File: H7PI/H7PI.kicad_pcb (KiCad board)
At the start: 4 copper layers, 65 x 30 mm, 52 parts, among them J1 XKTF-015-N, J10 DNP, J2 Header_2x10, J3 microUSB, J4 AFC07-S24ECA-00, J5 Header_2x20, J6 microUSB, J7 Header_1x2, J8 Header_1x1, J9 Header_1x1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

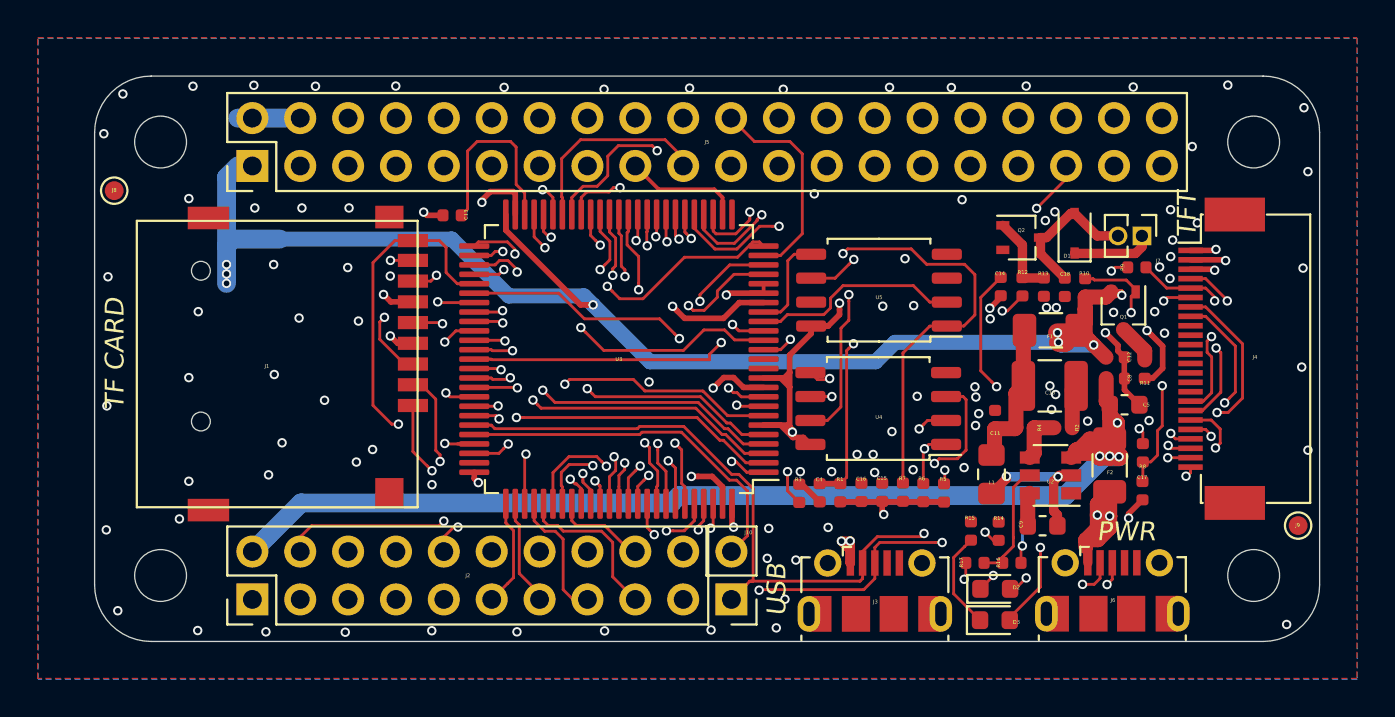
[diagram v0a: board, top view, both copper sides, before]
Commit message: v0.4 add pin info to bottom silk change pin name to Dx,Ax.
Signed-off-by: fuhua-chen <fuhua-chen@outlook.com>
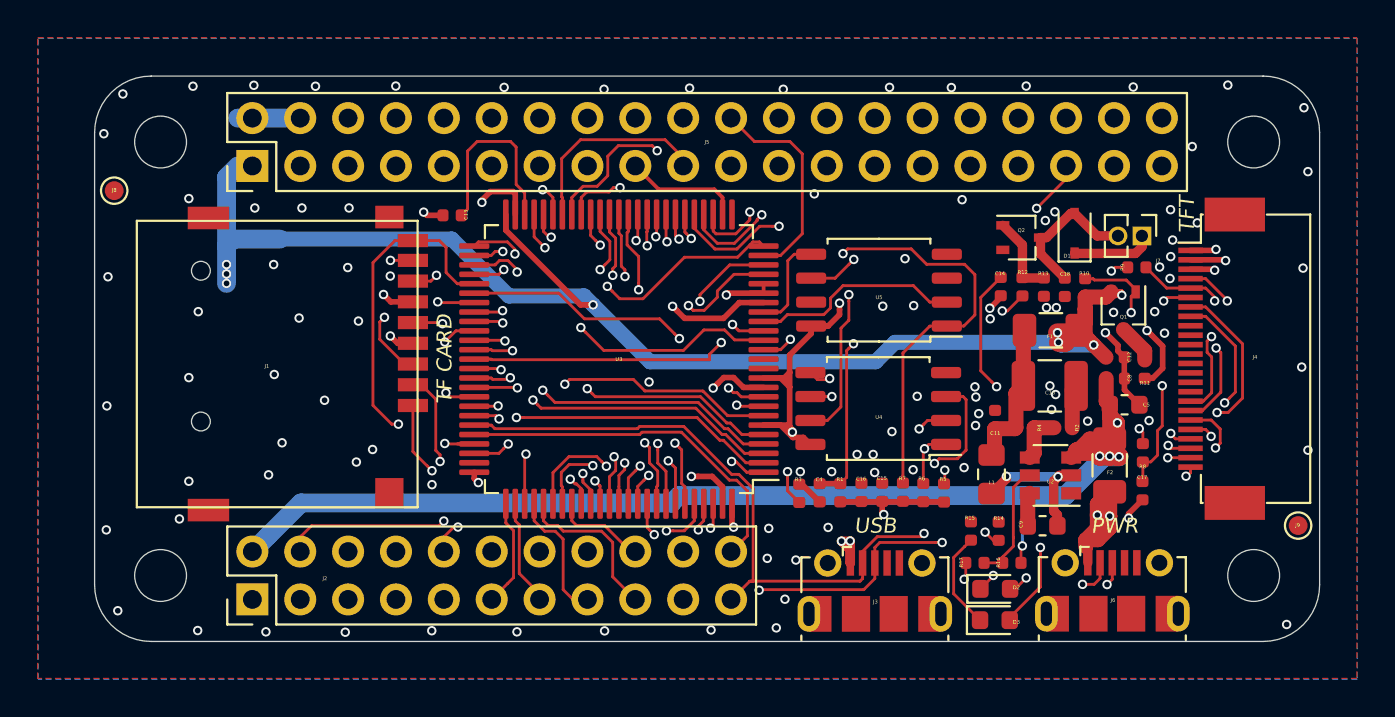
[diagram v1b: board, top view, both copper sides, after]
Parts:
- removed J10: DNP, PinHeader_1x02_P2.54mm_Vertical
- J2: value Header_2x10 -> Header_2x11; footprint PinHeader_2x10_P2.54mm_Vertical -> PinHeader_2x11_P2.54mm_Vertical
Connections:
- net /IO1 renamed /D8
- net /IO10 renamed /D17
- net /IO11 renamed /D18
- net /IO12 renamed /D19
- net /IO13 renamed /D20
- net /IO14 renamed /D21
- net /IO15 renamed /D22
- net /IO16 renamed /D23
- net /IO2 renamed /D9
- net /IO3 renamed /D10
- net /IO4 renamed /D11
- net /IO5 renamed /D12
- net /IO6 renamed /D13
- net /IO7 renamed /D14
- net /IO8 renamed /D15
- net /IO9 renamed /D16
- net /PI_CE0 renamed /CE0
- net /PI_CE1 renamed /CE1
- net /PI_GPIO0 renamed /D0
- net /PI_GPIO1 renamed /D1
- net /PI_GPIO2 renamed /D2
- net /PI_GPIO21 renamed /A0
- net /PI_GPIO22 renamed /A1
- net /PI_GPIO23 renamed /A2
- net /PI_GPIO24 renamed /A3
- net /PI_GPIO25 renamed /A4
- net /PI_GPIO26 renamed /A5
- net /PI_GPIO27 renamed /A6
- net /PI_GPIO28 renamed /A7
- net /PI_GPIO29 renamed /D29
- net /PI_GPIO3 renamed /D3
- net /PI_GPIO4 renamed /D4
- net /PI_GPIO5 renamed /D5
- net /PI_GPIO6 renamed /D6
- net /PI_GPIO7 renamed /D7
- net /PI_MISO renamed /MISO
- net /PI_MOSI renamed /MOSI
- net /PI_RXD renamed /RX0
- net /PI_SCK renamed /SCK
- net /PI_SCL0 renamed /SCL0
- net /PI_SCL1 renamed /SCL1
- net /PI_SDA0 renamed /SDA0
- net /PI_SDA1 renamed /SDA1
- net /PI_TXD renamed /TX0
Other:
- board text added: "3V3"
- board text added: "A0"
- board text added: "A1"
- board text added: "A2"
- board text added: "A3"
- board text added: "A4"
- board text added: "A5"
- board text added: "A6"
- board text added: "A7"
- board text added: "CE0"
- board text added: "CE1"
- board text added: "D0"
- board text added: "D1"
- board text added: "D10"
- board text added: "D11"
- board text added: "D12"
- board text added: "D13"
- board text added: "D14"
- board text added: "D15"
- board text added: "D16"
- board text added: "D17"
- board text added: "D18"
- board text added: "D19"
- board text added: "D2"
- board text added: "D20"
- board text added: "D21"
- board text added: "D22"
- board text added: "D23"
- board text added: "D29"
- board text added: "D3"
- board text added: "D4"
- board text added: "D5"
- board text added: "D6"
- board text added: "D7"
- board text added: "D8"
- board text added: "D9"
- board text added: "DN"
- board text added: "DP"
- board text added: "GND"
- board text added: "H7PI ZERO V0.4 20200116"
- board text added: "MISO"
- board text added: "MOSI"
- board text added: "RX0"
- board text added: "SCK"
- board text added: "SCL0"
- board text added: "SCL1"
- board text added: "SDA0"
- board text added: "SDA1"
- board text added: "TX0"
- board text added: "VBUS"
- board text removed: "H7PI ZERO V0.3 20191228"
